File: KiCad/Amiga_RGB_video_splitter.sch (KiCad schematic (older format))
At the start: 1 part, among them J2 DB23_Female-Connector

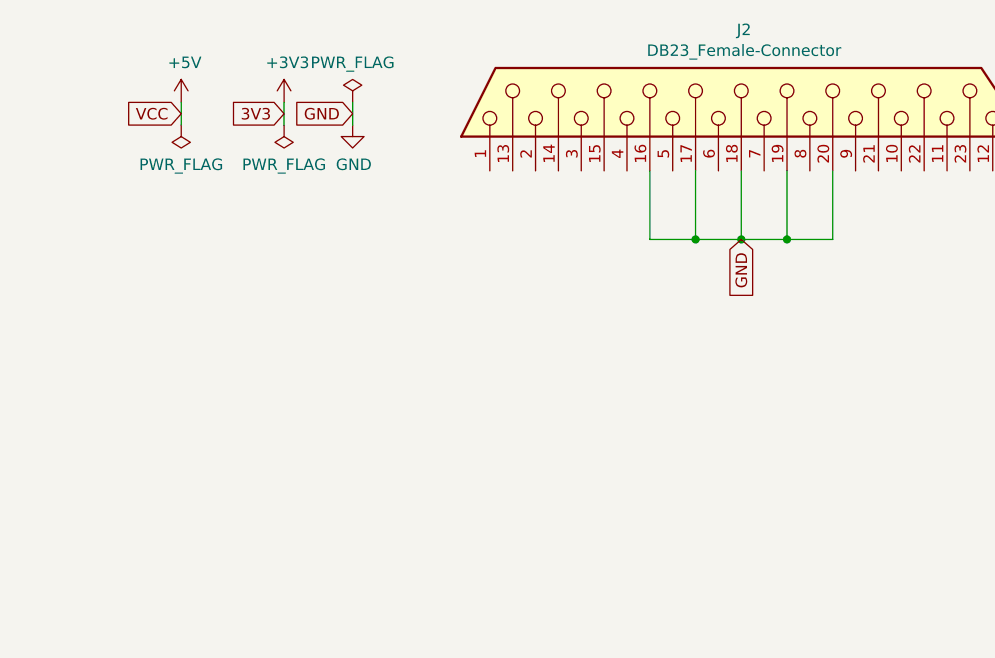
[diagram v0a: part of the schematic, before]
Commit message: Add symbol and place footprint for Connector_DB15_Female_HighDensity_MountingHoles
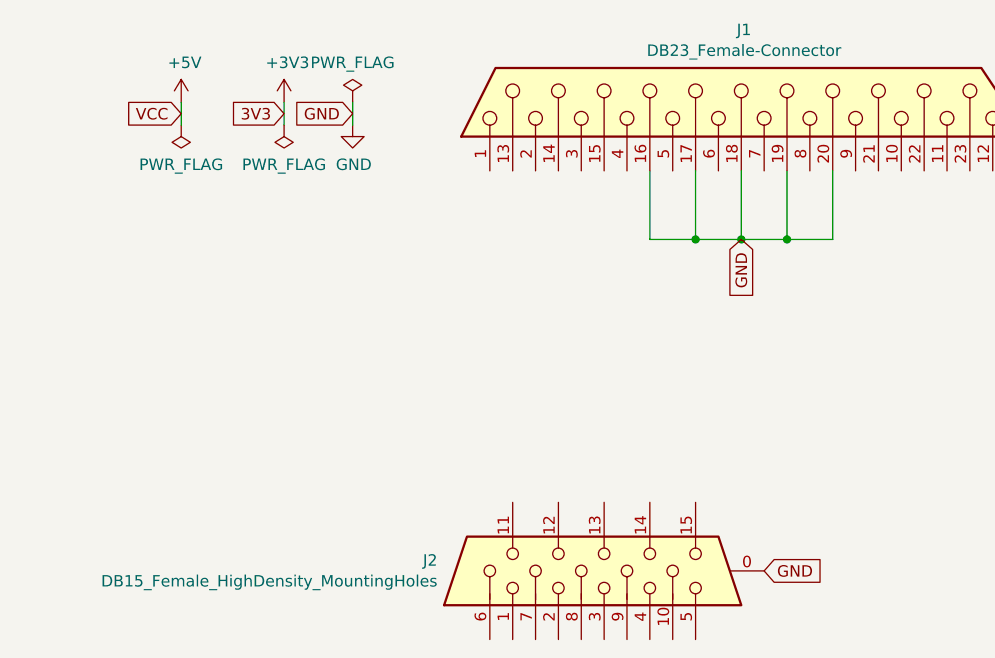
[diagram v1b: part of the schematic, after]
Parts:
- added J2: DB15_Female_HighDensity_MountingHoles, Connector_Dsub:DSUB-15-HD_Female_Horizontal_P2.29x1.98mm_EdgePinOffset3.03mm_Housed_MountingHolesOffset4.94mm, symbol Connector:DB15_Female_HighDensity_MountingHoles
- renumbered J2 to J1
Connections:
- net GND: now also J2.0
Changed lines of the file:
@@
 VCC
 $Comp
-L Amiga_RGB_video_splitter:DB23_Female-Connector J2
+L Amiga_RGB_video_splitter:DB23_Female-Connector J1
 U 1 1 682F1F1B
 P 3500 2400
-F 0 "J2" V 3817 2288 50  0000 C CNN
+F 0 "J1" V 3817 2288 50  0000 C CNN
 F 1 "DB23_Female-Connector" V 3726 2288 50  0000 C CNN
 F 2 "Amiga_RGB_video_splitter:DSUB-23_Female_EdgeMount_P2.77mm" H 3500 2200 50  0001 C CNN
@@
 Wire Wire Line
 	3400 3000 3600 3000
+$Comp
+L Connector:DB15_Female_HighDensity_MountingHoles J2
+U 1 1 683028A2
+P 3000 4450
+F 0 "J2" V 3046 5179 50  0000 L CNN
+F 1 "DB15_Female_HighDensity_MountingHoles" V 2955 5179 50  0000 L CNN
+F 2 "Connector_Dsub:DSUB-15-HD_Female_Horizontal_P2.29x1.98mm_EdgePinOffset3.03mm_Housed_MountingHolesOffset4.94mm" H 2050 4850 50  0001 C CNN
+F 3 " ~" H 2050 4850 50  0001 C CNN
+	1    3000 4450
+	0    -1   -1   0
+$EndComp
+Text GLabel 3700 4450 2    50   Input ~ 0
+GND
 $EndSCHEMATC

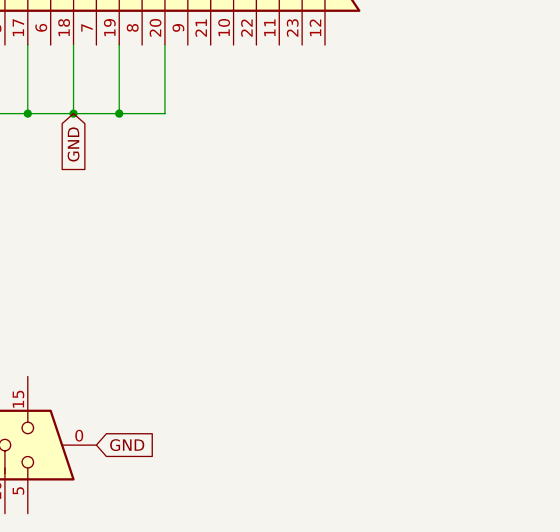
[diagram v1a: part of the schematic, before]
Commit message: Add Mini DIN 9 position receptacle connector
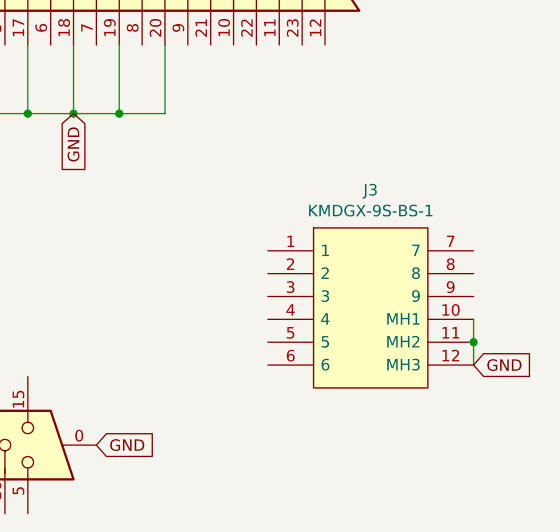
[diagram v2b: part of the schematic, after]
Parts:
- added J3: KMDGX-9S-BS-1, Amiga_RGB_video_splitter:KMDGX9SBS1, symbol Amiga_RGB_video_splitter:KMDGX-9S-BS-1
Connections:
- net GND: now also J3.10 (MH1), J3.11 (MH2), J3.12 (MH3)
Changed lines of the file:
@@
 Text GLabel 3700 4450 2    50   Input ~ 0
 GND
+$Comp
+L Amiga_RGB_video_splitter:KMDGX-9S-BS-1 J3
+U 1 1 6830CC46
+P 4900 3850
+F 0 "J3" H 4900 4365 50  0000 C CNN
+F 1 "KMDGX-9S-BS-1" H 4900 4274 50  0000 C CNN
+F 2 "Amiga_RGB_video_splitter:KMDGX9SBS1" H 4650 4250 50  0001 L CNN
+F 3 "https://www.kycon.com/Pub_Eng_Draw/KMDGX-9S-BS-1.pdf" H 5200 4100 50  0001 L CNN
+	1    4900 3850
+	1    0    0    -1
+$EndComp
+Text GLabel 5350 4100 2    50   Input ~ 0
+GND
+Wire Wire Line
+	5350 3900 5350 4000
+Wire Wire Line
+	5350 4000 5350 4100
+Connection ~ 5350 4000
 $EndSCHEMATC

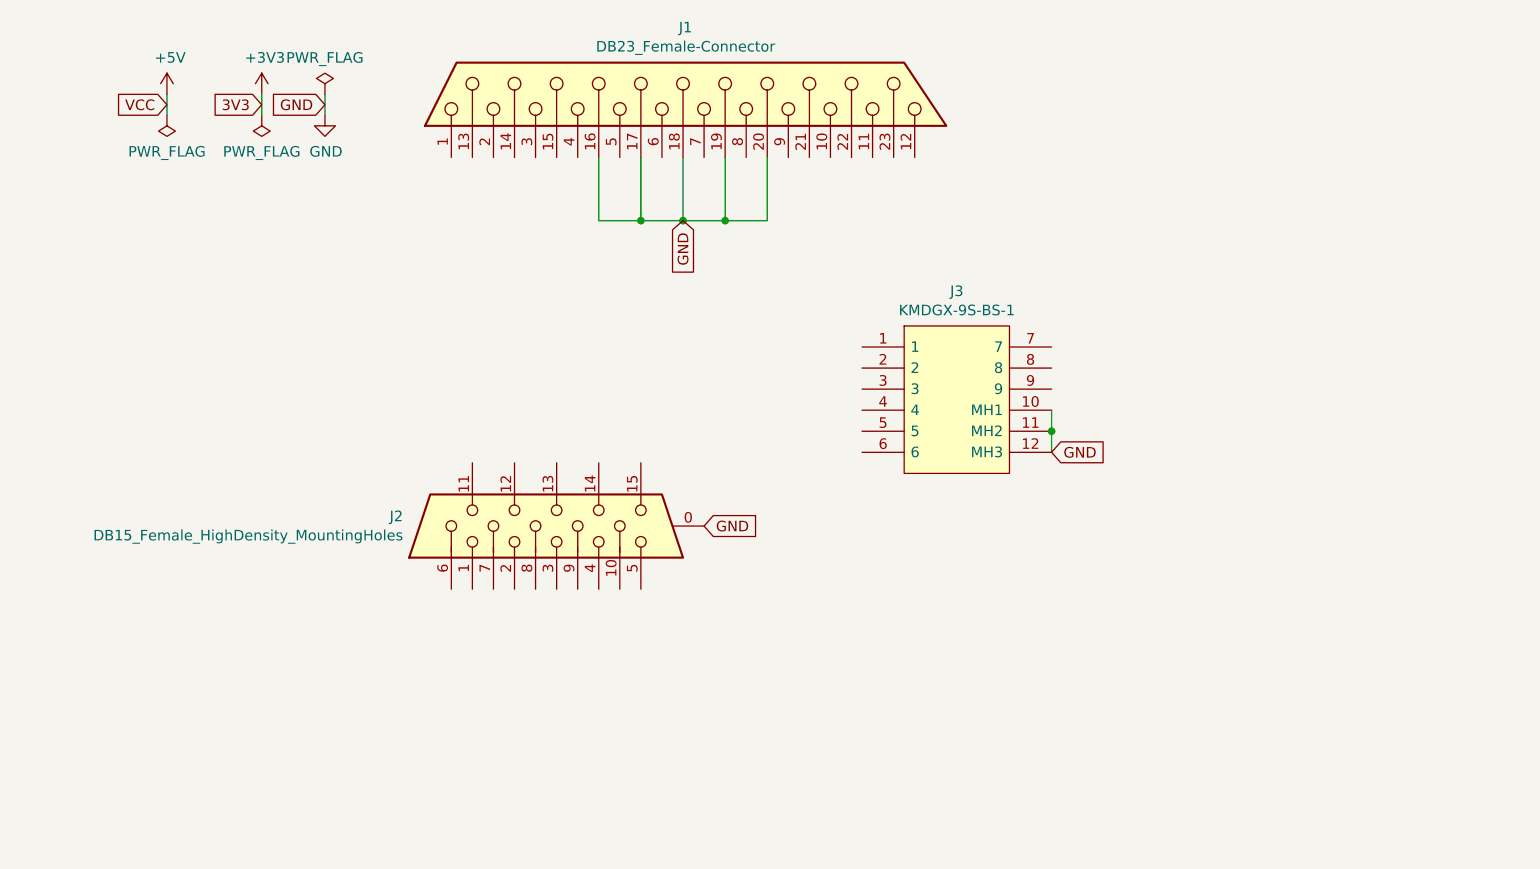
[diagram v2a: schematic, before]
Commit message: Add a PJ-320A stereo input connector to the design
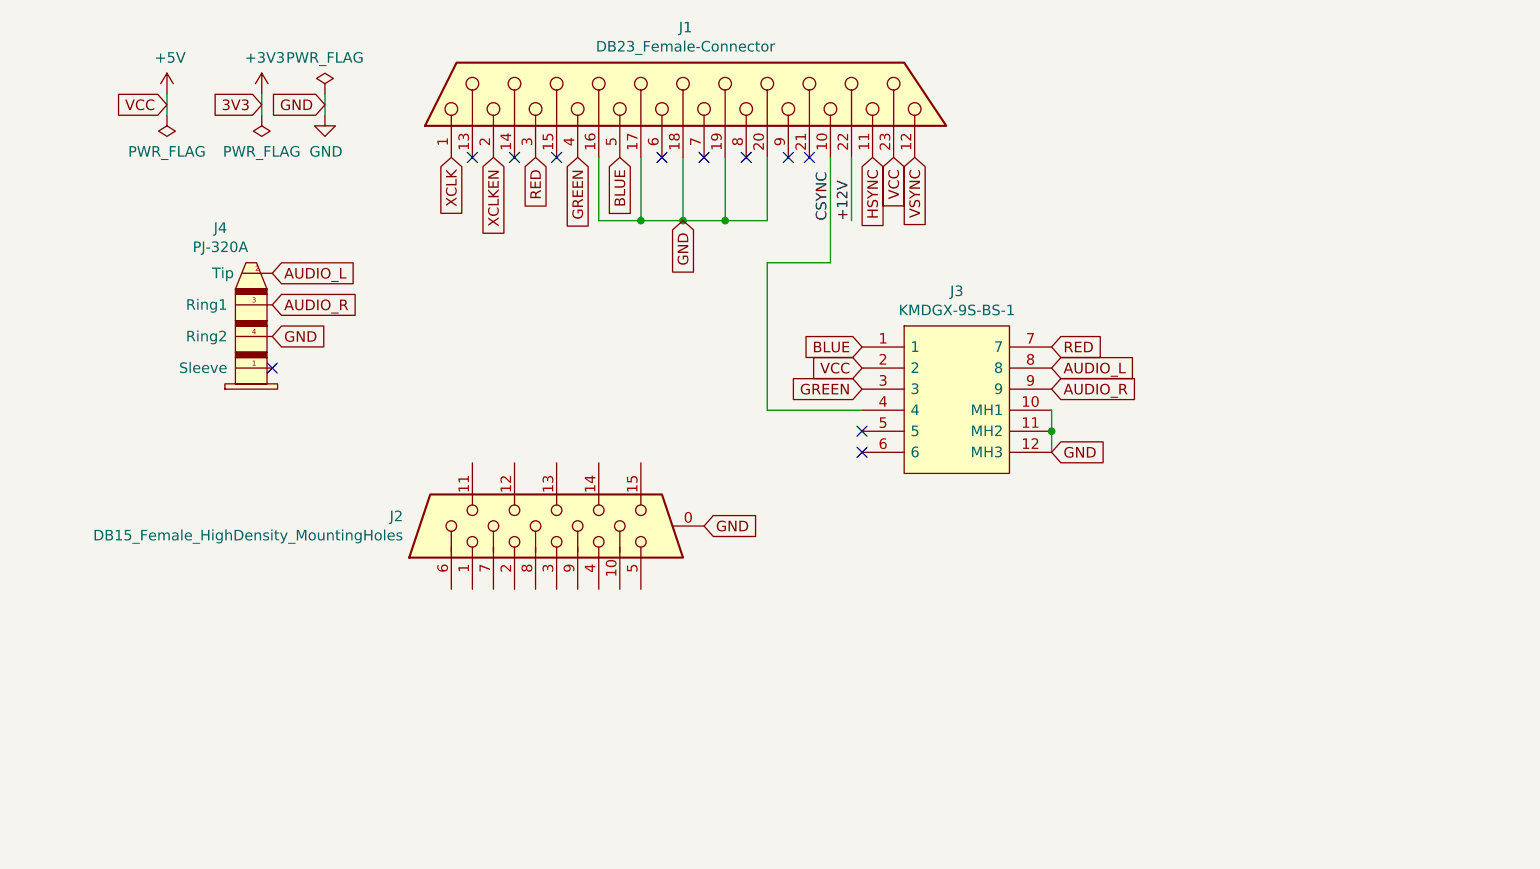
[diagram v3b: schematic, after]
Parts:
- added J4: PJ-320A, Amiga_RGB_video_splitter:PJ-320A, symbol Amiga_RGB_video_splitter:PJ-320A
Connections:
- net +5V: now also J1.23, J3.2
- net GND: now also J4.4 (Ring2)
- net XCLK: now reaches J1.1
- net CSYNC: now reaches J1.10
- net CSYNC: now also J3.4
- net HSYNC: now reaches J1.11
- net VSYNC: now reaches J1.12
- net XCLKEN: now reaches J1.2
- net +12V: now reaches J1.22
- net RED: now reaches J1.3
- net RED: now also J3.7
- net GREEN: now reaches J1.4
- net GREEN: now also J3.3
- net BLUE: now reaches J1.5
- net BLUE: now also J3.1
- net AUDIO_L: now reaches J3.8
- net AUDIO_L: now also J4.2 (Tip)
- net AUDIO_R: now reaches J3.9
- net AUDIO_R: now also J4.3 (Ring1)
- no-connect marks 0 -> 11
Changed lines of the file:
@@
 	5350 4000 5350 4100
 Connection ~ 5350 4000
+Text GLabel 4600 2700 3    50   Input ~ 0
+VCC
+Text GLabel 2900 2700 3    50   Input ~ 0
+RED
+Text GLabel 3100 2700 3    50   Input ~ 0
+GREEN
+Text GLabel 3300 2700 3    50   Input ~ 0
+BLUE
+Text GLabel 2500 2700 3    50   Input ~ 0
+XCLK
+Text GLabel 2700 2700 3    50   Input ~ 0
+XCLKEN
+NoConn ~ 2600 2700
+NoConn ~ 2800 2700
+NoConn ~ 3000 2700
+NoConn ~ 3500 2700
+NoConn ~ 3700 2700
+NoConn ~ 3900 2700
+NoConn ~ 4100 2700
+NoConn ~ 4200 2700
+Text Label 4300 3000 1    50   ~ 0
+CSYNC
+Wire Wire Line
+	4400 2700 4400 3000
+Text Label 4400 3000 1    50   ~ 0
++12V
+Text GLabel 4500 2700 3    50   Input ~ 0
+HSYNC
+Text GLabel 4700 2700 3    50   Input ~ 0
+VSYNC
+Text GLabel 5350 3600 2    50   Input ~ 0
+RED
+Text GLabel 4450 3800 0    50   Input ~ 0
+GREEN
+Text GLabel 4450 3600 0    50   Input ~ 0
+BLUE
+Text GLabel 4450 3700 0    50   Input ~ 0
+VCC
+Wire Wire Line
+	4450 3900 4000 3900
+Wire Wire Line
+	4000 3900 4000 3200
+Wire Wire Line
+	4000 3200 4300 3200
+Wire Wire Line
+	4300 2700 4300 3200
+NoConn ~ 4450 4000
+NoConn ~ 4450 4100
+Text GLabel 5350 3800 2    50   Input ~ 0
+AUDIO_R
+Text GLabel 5350 3700 2    50   Input ~ 0
+AUDIO_L
+$Comp
+L Amiga_RGB_video_splitter:PJ-320A J4
+U 1 1 68306894
+P 1550 3850
+F 0 "J4" H 1404 4665 50  0000 C CNN
+F 1 "PJ-320A" H 1404 4574 50  0000 C CNN
+F 2 "Amiga_RGB_video_splitter:PJ-320A" H 1550 3850 50  0001 C CNN
+F 3 "" H 1550 3850 50  0001 C CNN
+	1    1550 3850
+	1    0    0    -1
+$EndComp
+Text GLabel 1650 3250 2    50   Input ~ 0
+AUDIO_L
+Text GLabel 1650 3400 2    50   Input ~ 0
+AUDIO_R
+Text GLabel 1650 3550 2    50   Input ~ 0
+GND
+NoConn ~ 1650 3700
 $EndSCHEMATC

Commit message: Add THS7374IPWR to the design and temporary routing
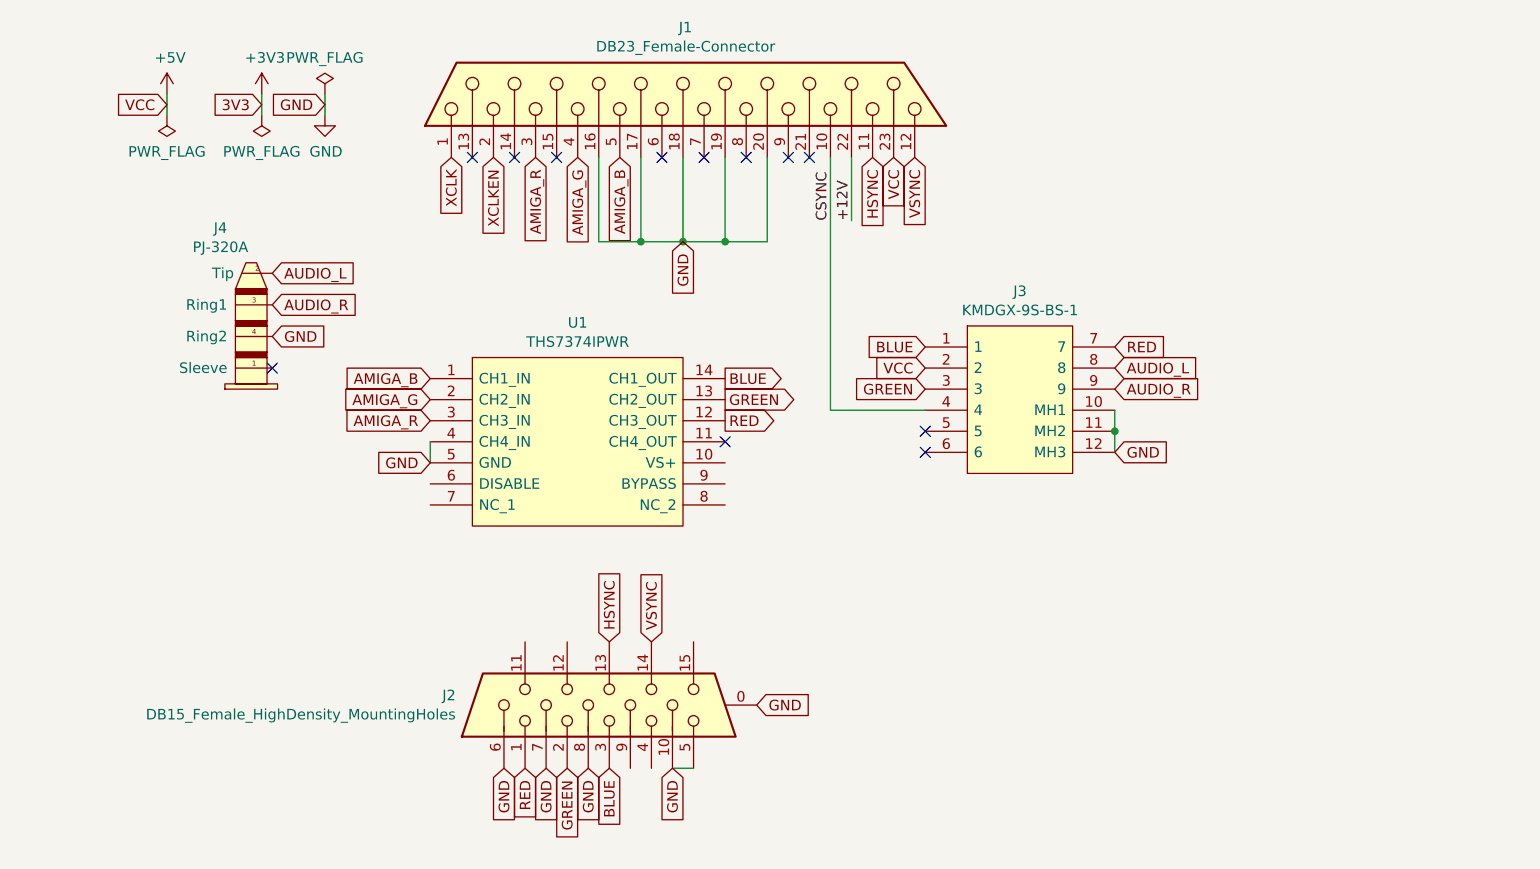
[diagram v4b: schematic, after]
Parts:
- added U1: THS7374IPWR, Package_SO:TSSOP-14_4.4x5mm_P0.65mm, symbol Amiga_RGB_video_splitter:THS7374IPWR
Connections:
- net BLUE: now also J2.3, U1.14 (CH1_OUT); no longer J1.5
- net GND: now also J2.10, J2.5, J2.6, J2.7, J2.8, U1.4 (CH4_IN), U1.5 (GND)
- net GREEN: now also J2.2, U1.13 (CH2_OUT); no longer J1.4
- net HSYNC: now also J2.13
- net RED: now also J2.1, U1.12 (CH3_OUT); no longer J1.3
- net VSYNC: now also J2.14
- new net AMIGA_B: J1.5, U1.1 (CH1_IN)
- new net AMIGA_G: J1.4, U1.2 (CH2_IN)
- new net AMIGA_R: J1.3, U1.3 (CH3_IN)
- no-connect marks 11 -> 12
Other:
- moved on the sheet: J2, J3
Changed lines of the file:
@@
 	0    -1   -1   0
 $EndComp
-Text GLabel 3600 3000 3    50   Input ~ 0
+Text GLabel 3600 3100 3    50   Input ~ 0
 GND
 Wire Wire Line
-	3200 2700 3200 3000
+	3200 3100 3400 3100
+Connection ~ 3800 3100
 Wire Wire Line
-	3200 3000 3400 3000
+	3800 3100 4000 3100
+Connection ~ 3600 3100
 Wire Wire Line
-	4000 3000 4000 2700
+	3600 3100 3800 3100
+Connection ~ 3400 3100
 Wire Wire Line
-	3800 2700 3800 3000
-Connection ~ 3800 3000
-Wire Wire Line
-	3800 3000 4000 3000
-Wire Wire Line
-	3600 2700 3600 3000
-Connection ~ 3600 3000
-Wire Wire Line
-	3600 3000 3800 3000
-Wire Wire Line
-	3400 2700 3400 3000
-Connection ~ 3400 3000
-Wire Wire Line
-	3400 3000 3600 3000
+	3400 3100 3600 3100
 $Comp
 L Connector:DB15_Female_HighDensity_MountingHoles J2
 U 1 1 683028A2
-P 3000 4450
-F 0 "J2" V 3046 5179 50  0000 L CNN
-F 1 "DB15_Female_HighDensity_MountingHoles" V 2955 5179 50  0000 L CNN
-F 2 "Connector_Dsub:DSUB-15-HD_Female_Horizontal_P2.29x1.98mm_EdgePinOffset3.03mm_Housed_MountingHolesOffset4.94mm" H 2050 4850 50  0001 C CNN
-F 3 " ~" H 2050 4850 50  0001 C CNN
-	1    3000 4450
+P 3250 5300
+F 0 "J2" V 3296 6029 50  0000 L CNN
+F 1 "DB15_Female_HighDensity_MountingHoles" V 3205 6029 50  0000 L CNN
+F 2 "Connector_Dsub:DSUB-15-HD_Female_Horizontal_P2.29x1.98mm_EdgePinOffset3.03mm_Housed_MountingHolesOffset4.94mm" H 2300 5700 50  0001 C CNN
+F 3 " ~" H 2300 5700 50  0001 C CNN
+	1    3250 5300
 	0    -1   -1   0
 $EndComp
-Text GLabel 3700 4450 2    50   Input ~ 0
+Text GLabel 3950 5300 2    50   Input ~ 0
 GND
 $Comp
 L Amiga_RGB_video_splitter:KMDGX-9S-BS-1 J3
 U 1 1 6830CC46
-P 4900 3850
-F 0 "J3" H 4900 4365 50  0000 C CNN
-F 1 "KMDGX-9S-BS-1" H 4900 4274 50  0000 C CNN
-F 2 "Amiga_RGB_video_splitter:KMDGX9SBS1" H 4650 4250 50  0001 L CNN
-F 3 "https://www.kycon.com/Pub_Eng_Draw/KMDGX-9S-BS-1.pdf" H 5200 4100 50  0001 L CNN
-	1    4900 3850
+P 5200 3850
+F 0 "J3" H 5200 4365 50  0000 C CNN
+F 1 "KMDGX-9S-BS-1" H 5200 4274 50  0000 C CNN
+F 2 "Amiga_RGB_video_splitter:KMDGX9SBS1" H 4950 4250 50  0001 L CNN
+F 3 "https://www.kycon.com/Pub_Eng_Draw/KMDGX-9S-BS-1.pdf" H 5500 4100 50  0001 L CNN
+	1    5200 3850
 	1    0    0    -1
 $EndComp
-Text GLabel 5350 4100 2    50   Input ~ 0
+Text GLabel 5650 4100 2    50   Input ~ 0
 GND
 Wire Wire Line
-	5350 3900 5350 4000
+	5650 3900 5650 4000
 Wire Wire Line
-	5350 4000 5350 4100
-Connection ~ 5350 4000
+	5650 4000 5650 4100
+Connection ~ 5650 4000
 Text GLabel 4600 2700 3    50   Input ~ 0
 VCC
 Text GLabel 2900 2700 3    50   Input ~ 0
-RED
+AMIGA_R
 Text GLabel 3100 2700 3    50   Input ~ 0
-GREEN
+AMIGA_G
 Text GLabel 3300 2700 3    50   Input ~ 0
-BLUE
+AMIGA_B
 Text GLabel 2500 2700 3    50   Input ~ 0
 XCLK
@@
 Text GLabel 4700 2700 3    50   Input ~ 0
 VSYNC
-Text GLabel 5350 3600 2    50   Input ~ 0
+Text GLabel 5650 3600 2    50   Input ~ 0
 RED
-Text GLabel 4450 3800 0    50   Input ~ 0
+Text GLabel 4750 3800 0    50   Input ~ 0
 GREEN
-Text GLabel 4450 3600 0    50   Input ~ 0
+Text GLabel 4750 3600 0    50   Input ~ 0
 BLUE
-Text GLabel 4450 3700 0    50   Input ~ 0
+Text GLabel 4750 3700 0    50   Input ~ 0
 VCC
 Wire Wire Line
-	4450 3900 4000 3900
-Wire Wire Line
-	4000 3900 4000 3200
-Wire Wire Line
-	4000 3200 4300 3200
-Wire Wire Line
-	4300 2700 4300 3200
-NoConn ~ 4450 4000
-NoConn ~ 4450 4100
-Text GLabel 5350 3800 2    50   Input ~ 0
+	4750 3900 4300 3900
+NoConn ~ 4750 4000
+NoConn ~ 4750 4100
+Text GLabel 5650 3800 2    50   Input ~ 0
 AUDIO_R
-Text GLabel 5350 3700 2    50   Input ~ 0
+Text GLabel 5650 3700 2    50   Input ~ 0
 AUDIO_L
 $Comp
@@
 GND
 NoConn ~ 1650 3700
+Wire Wire Line
+	4300 2700 4300 3900
+$Comp
+L Amiga_RGB_video_splitter:THS7374IPWR U1
+U 1 1 683153B1
+P 3100 4050
+F 0 "U1" H 3100 4615 50  0000 C CNN
+F 1 "THS7374IPWR" H 3100 4524 50  0000 C CNN
+F 2 "Package_SO:TSSOP-14_4.4x5mm_P0.65mm" H 3650 4450 50  0001 L CNN
+F 3 "http://www.ti.com/lit/ds/symlink/ths7374.pdf" H 3650 4350 50  0001 L CNN
+	1    3100 4050
+	1    0    0    -1
+$EndComp
+Text GLabel 2400 4150 0    50   Input ~ 0
+GND
+Text GLabel 3800 3950 2    50   Output ~ 0
+RED
+Text GLabel 3800 3850 2    50   Output ~ 0
+GREEN
+Wire Wire Line
+	2400 4050 2400 4150
+NoConn ~ 3800 4050
+Wire Wire Line
+	3600 2700 3600 3100
+Wire Wire Line
+	3200 2700 3200 3100
+Wire Wire Line
+	3400 2700 3400 3100
+Wire Wire Line
+	3800 2700 3800 3100
+Wire Wire Line
+	4000 2700 4000 3100
+Text GLabel 3800 3750 2    50   Output ~ 0
+BLUE
+Text GLabel 2400 3850 0    50   Input ~ 0
+AMIGA_G
+Text GLabel 2400 3950 0    50   Input ~ 0
+AMIGA_R
+Text GLabel 2400 3750 0    50   Input ~ 0
+AMIGA_B
+Text GLabel 2850 5600 3    50   Input ~ 0
+RED
+Text GLabel 3050 5600 3    50   Input ~ 0
+GREEN
+Text GLabel 3250 5600 3    50   Input ~ 0
+BLUE
+Text GLabel 2750 5600 3    50   Input ~ 0
+GND
+Text GLabel 2950 5600 3    50   Input ~ 0
+GND
+Text GLabel 3150 5600 3    50   Input ~ 0
+GND
+Text GLabel 3250 5000 1    50   Input ~ 0
+HSYNC
+Text GLabel 3450 5000 1    50   Input ~ 0
+VSYNC
+Text GLabel 3550 5600 3    50   Input ~ 0
+GND
+Wire Wire Line
+	3550 5600 3650 5600
 $EndSCHEMATC
